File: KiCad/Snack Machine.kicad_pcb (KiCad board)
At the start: 2 copper layers, 107.5 x 100 mm, 314 parts, among them J1 MDB, J10 Row Screw Terminal, J11 Column Screw Terminal, J12 Display Serial Header, J13 RFID_CONNECTOR, J14 Large Display Header, J16 USB_B_Micro, J17 AVR-ISP-6, J18 Conn_02x02_Odd_Even, J2 Power Screw Terminal, J3 RFID Serial Connector, J4 RFID Led Connector, J5 MDB, J6 Conn_01x02, J7 LCD EXP1, J8 LCD EXP2, J9 AVR-ISP-6, Q1 P-CH 30V 3.8A, Q10 MMBT3904, Q11 P-CH 30V 3.8A, Q12 P-CH 30V 3.8A, Q13 P-CH 30V 3.8A, Q14 P-CH 30V 3.8A, Q15 MMBT3904, Q16 MMBT3904, Q17 MMBT3904, Q18 MMBT3904, Q19 Q_NMOS_SGD, Q2 Q_NMOS_SGD, Q20 Q_NMOS_SGD, Q21 Q_NMOS_SGD, Q22 Q_NMOS_SGD, Q23 Q_NMOS_SGD, Q24 Q_NMOS_SGD, Q25 Q_NMOS_SGD, Q3 P-CH 30V 3.8A, Q4 P-CH 30V 3.8A, Q5 P-CH 30V 3.8A, Q6 P-CH 30V 3.8A, Q7 MMBT3904, Q8 MMBT3904, Q9 MMBT3904, SW1 SW_SPST, U1 MEZD71201A-F, U2 MEZD71202A-G, U3 ATmega2560-16AU, U4 INA180B3, U5 INA219, U6 ATmega16U2-MU, U7 74AHC1G125, U8 W5500, U9 RB1-125BAG1A, Y1 16MHz, Y2 16MHz, Y3 25MHz

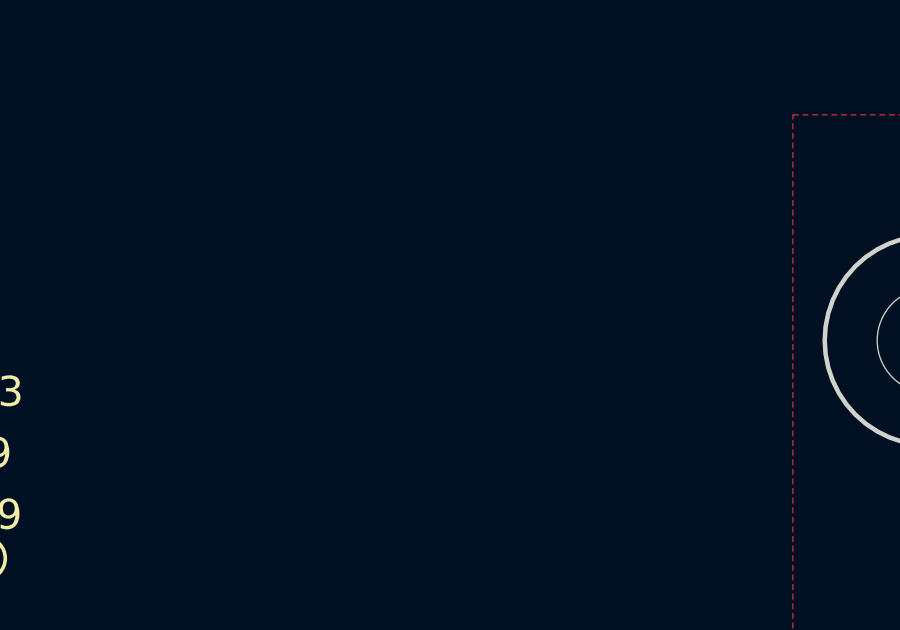
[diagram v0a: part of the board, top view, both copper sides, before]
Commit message: added one resistor, about to rip up all traces and move all the parts around
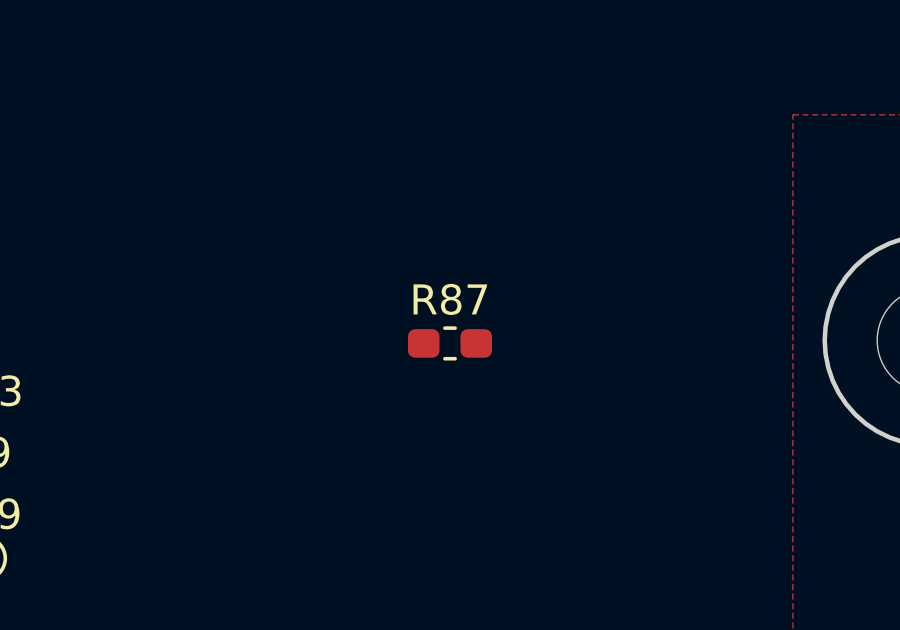
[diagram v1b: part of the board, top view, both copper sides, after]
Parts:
- added R87: OPEN, Resistor_SMD:R_0603_1608Metric_Pad1.05x0.95mm_HandSolder, F.Cu at (80.0, 57.1)
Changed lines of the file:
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@@
     (tracks 971)
     (zones 0)
-    (modules 314)
+    (modules 315)
     (nets 283)
   )
@@
       (at (xyz 0 0 0))
       (scale (xyz 1 1 1))
+      (rotate (xyz 0 0 0))
+    )
+  )
+  (module Resistor_SMD:R_0603_1608Metric_Pad1.05x0.95mm_HandSolder (layer F.Cu)
+    (at 80.01 57.15)
+    (descr "Resistor SMD 0603 (1608 Metric), square (rectangular) end terminal, IPC_7351 nominal with elongated pad for handsoldering. (Body size source: http://www.tortai-tech.com/upload/download/2011102023233369053.pdf), generated with kicad-footprint-generator")
+    (tags "resistor handsolder")
+    (attr smd)
+    (fp_text reference R87 (at 0 -1.43) (layer F.SilkS)
+      (effects (font (size 1 1) (thickness 0.15)))
+    )
+    (fp_text value OPEN (at 0 1.43) (layer F.Fab)
+      (effects (font (size 1 1) (thickness 0.15)))
+    )
+    (fp_line (start -0.8 0.4) (end -0.8 -0.4) (layer F.Fab) (width 0.1))
+    (fp_line (start -0.8 -0.4) (end 0.8 -0.4) (layer F.Fab) (width 0.1))
+    (fp_line (start 0.8 -0.4) (end 0.8 0.4) (layer F.Fab) (width 0.1))
+    (fp_line (start 0.8 0.4) (end -0.8 0.4) (layer F.Fab) (width 0.1))
+    (fp_line (start -0.171267 -0.51) (end 0.171267 -0.51) (layer F.SilkS) (width 0.12))
+    (fp_line (start -0.171267 0.51) (end 0.171267 0.51) (layer F.SilkS) (width 0.12))
+    (fp_line (start -1.65 0.73) (end -1.65 -0.73) (layer F.CrtYd) (width 0.05))
+    (fp_line (start -1.65 -0.73) (end 1.65 -0.73) (layer F.CrtYd) (width 0.05))
+    (fp_line (start 1.65 -0.73) (end 1.65 0.73) (layer F.CrtYd) (width 0.05))
+    (fp_line (start 1.65 0.73) (end -1.65 0.73) (layer F.CrtYd) (width 0.05))
+    (fp_text user %R (at 0 0) (layer F.Fab)
+      (effects (font (size 0.4 0.4) (thickness 0.06)))
+    )
+    (pad 1 smd roundrect (at -0.875 0) (size 1.05 0.95) (layers F.Cu F.Paste F.Mask) (roundrect_rratio 0.25)
+      (net 53 /MISO))
+    (pad 2 smd roundrect (at 0.875 0) (size 1.05 0.95) (layers F.Cu F.Paste F.Mask) (roundrect_rratio 0.25)
+      (net 214 /Ethernet/MISO_TRISTATE))
+    (model ${KISYS3DMOD}/Resistor_SMD.3dshapes/R_0603_1608Metric.wrl
+      (at (xyz 0 0 0))
+      (scale (xyz 1 1 1))

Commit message: rearranging footprints on layout
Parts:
- TP1, TP10, TP11, TP12, TP13, TP14, TP15, TP16, TP17, TP18, TP19, TP2, TP20, TP21, TP22, TP23, TP24, TP25, TP26, TP27, TP28, TP29, TP3, TP30, TP31, TP32, TP33, TP34, TP35, TP36, TP37, TP38, TP39, TP4, TP40, TP41, TP42, TP43, TP44, TP45, TP46, TP47, TP48, TP49, TP5, TP50, TP51, TP52, TP53, TP54, TP55, TP56, TP57, TP58, TP59, TP6, TP60, TP61, TP62, TP63, TP64, TP65, TP66, TP67, TP68, TP69, TP7, TP70, TP71, TP72, TP73, TP74, TP75, TP76, TP77, TP78, TP79, TP8, TP80, TP81, TP82, TP83, TP84, TP85, TP86, TP87, TP88, TP89, TP9, TP90, TP91, TP92, TP93: footprint TestPoint:TestPoint_THTPad_D1.0mm_Drill0.5mm -> Snack Machine:TestPoint_THTPad_D0.8mm_Drill0.4mm
- moved C45 194.5 mm to (66.3, 74.2)
- moved Y3 191.1 mm to (57.7, 123.2)
- moved R80 185.2 mm to (81.0, 173.5)
- moved R81 185.2 mm to (84.3, 172.0)
- moved R82 185.2 mm to (81.0, 175.0)
- moved R83 185.2 mm to (84.3, 173.5)
- moved R85 185.2 mm to (84.3, 175.0)
- moved R84 185.2 mm to (87.7, 172.0)
- moved R86 185.2 mm to (87.7, 173.5)
- moved R79 184.6 mm to (80.6, 170.8)
- moved FB2 183.4 mm to (70.2, 126.5)
- moved FB3 175.7 mm to (77.9, 126.2)
- moved TP1 162.8 mm to (108.1, 40.9)
- moved D4 159.2 mm to (280.7, 148.2)
- moved R59 159.2 mm to (285.9, 152.1)
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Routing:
- net +5V: track 106.7 -> 0.00 mm, vias 1 -> 0
- net /SCL: track 87.9 -> 0.00 mm, vias 3 -> 0
- net /SDA: track 82.3 -> 0.00 mm, vias 3 -> 0
- net /r1: track 70.3 -> 0.00 mm
- net /MOSI: track 65.9 -> 0.00 mm, vias 2 -> 0
- net /r2: track 65.1 -> 0.00 mm
- net /SCK: track 63.3 -> 0.00 mm, vias 2 -> 0
- net GND: track 62.8 -> 0.00 mm, vias 3 -> 0
- net /r3: track 62.2 -> 0.00 mm
- net /DOOR_SW: track 60.7 -> 0.00 mm, vias 1 -> 0
- net /r4: track 56.1 -> 0.00 mm
- net /r5: track 51.5 -> 0.00 mm
- net +24V: track 51.0 -> 0.00 mm
- net Net-(C7-Pad1): track 47.1 -> 0.00 mm, vias 1 -> 0
- net Net-(C9-Pad1): track 46.4 -> 0.00 mm, vias 1 -> 0
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
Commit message: moving stuff around
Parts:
- C45, R65, R74, R76, R87, U7: moved to B.Cu
- U1, U2: footprint Connector_PinHeader_2.54mm:PinHeader_1x03_P2.54mm_Vertical -> Snack Machine:mEZD71201A
- moved C24 229.7 mm to (32.7, 145.4)
- moved C27 229.7 mm to (34.2, 140.3)
- moved C29 229.7 mm to (40.2, 146.9)
- moved D4 229.7 mm to (51.0, 149.9)
- moved J17 229.7 mm to (56.0, 140.6)
- moved R59 229.7 mm to (56.2, 153.8)
- moved R60 229.7 mm to (56.2, 152.0)
- moved U6 229.7 mm to (38.8, 141.8)
- moved C18 229.7 mm to (61.1, 153.9)
- moved C20 229.7 mm to (61.1, 152.0)
- moved C23 229.7 mm to (33.2, 152.2)
- moved C25 229.7 mm to (40.8, 152.2)
- moved C26 229.7 mm to (30.6, 145.4)
- moved C28 229.7 mm to (40.8, 148.8)
- moved C30 229.7 mm to (51.5, 144.4)
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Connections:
- Y3 pad 2: Net-(C32-Pad1) -> GND
- Y3 pad 3: (no net) -> Net-(C32-Pad1)
- Y3 pad 4: (no net) -> GND

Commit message: Moved stuff around on the layout, still need to fanout the large processor, place the power regulators, place the door switch connector, place the RFID connectors, and place the LCD connectors.  Once all parts are placed, routing can begin.
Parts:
- C23, C25, C27, C28, C29, C46, C47, C48, C49, C50, C51, C52, C53, D5, D6, R55, R56, R57, R59, R60, R61, R62, R63, R79, R80, R81, R82, R83, R84, R85, R86, U6, Y2: moved to B.Cu
- moved C1 154.5 mm to (85.6, 129.2)
- moved C3 154.5 mm to (72.9, 129.2)
- moved D7 154.5 mm to (78.2, 124.3)
- moved TP85 154.5 mm to (86.7, 134.6)
- moved TP87 154.5 mm to (89.0, 134.0)
- moved D8 154.5 mm to (78.4, 121.7)
- moved U2 154.5 mm to (81.8, 127.9)
- moved R82 132.8 mm to (180.1, 86.7), turned to 180 degrees
- moved R85 129.7 mm to (182.9, 90.8), turned to 270 degrees
- moved R86 129.4 mm to (182.9, 85.9), turned to 270 degrees
- moved R80 125.4 mm to (180.1, 96.6), turned to 180 degrees
- moved R81 125.0 mm to (180.1, 91.7), turned to 180 degrees
- moved R83 122.5 mm to (182.9, 100.8), turned to 270 degrees
- moved R84 122.0 mm to (182.9, 95.8), turned to 270 degrees
- moved R79 121.1 mm to (180.1, 101.7)
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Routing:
- net /r8: vias 1 -> 0
- net /r7: vias 1 -> 0
- net /r6: vias 1 -> 0
- net /r5: vias 1 -> 0
- net /r4: vias 1 -> 0
- net /r3: vias 1 -> 0
- net /r2: vias 1 -> 0
- net /r1: vias 1 -> 0
- net /c7: vias 1 -> 0
- net /c6: vias 1 -> 0
- net /c5: vias 1 -> 0
- net /c4: vias 1 -> 0
- net /c3: vias 1 -> 0
- net /c2: vias 1 -> 0
- net /c1: vias 1 -> 0
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
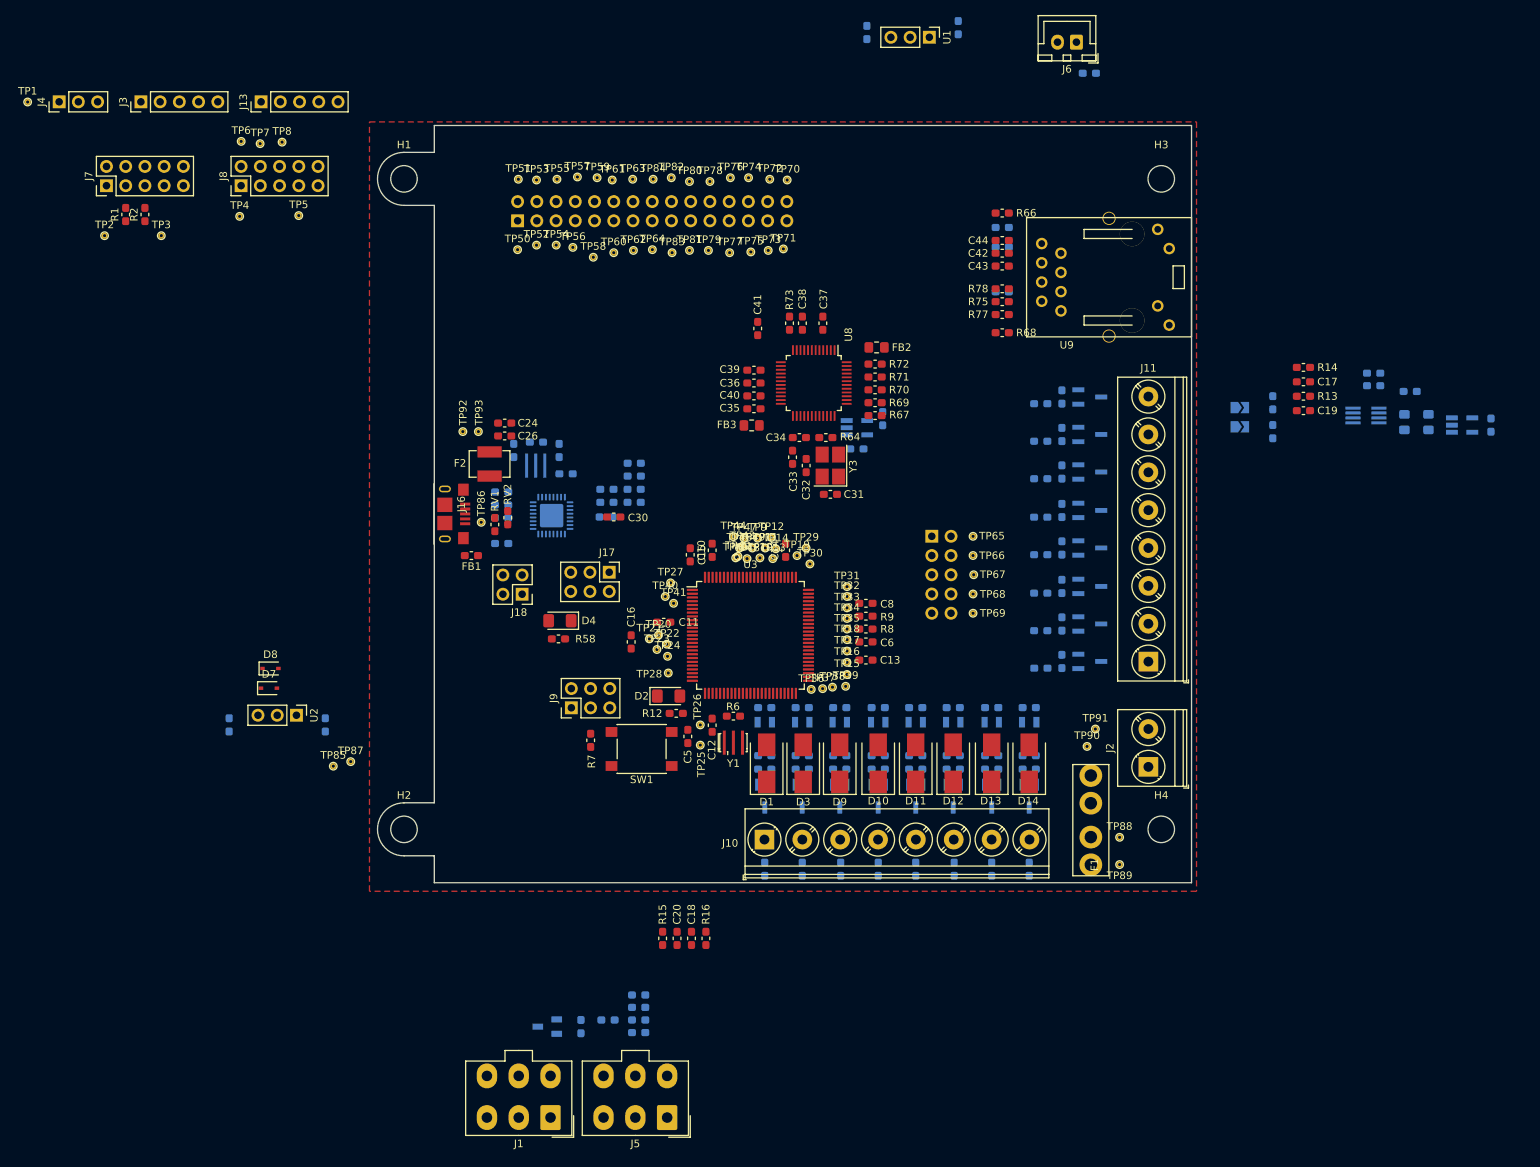
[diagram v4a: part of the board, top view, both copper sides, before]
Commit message: all parts placed within board outline
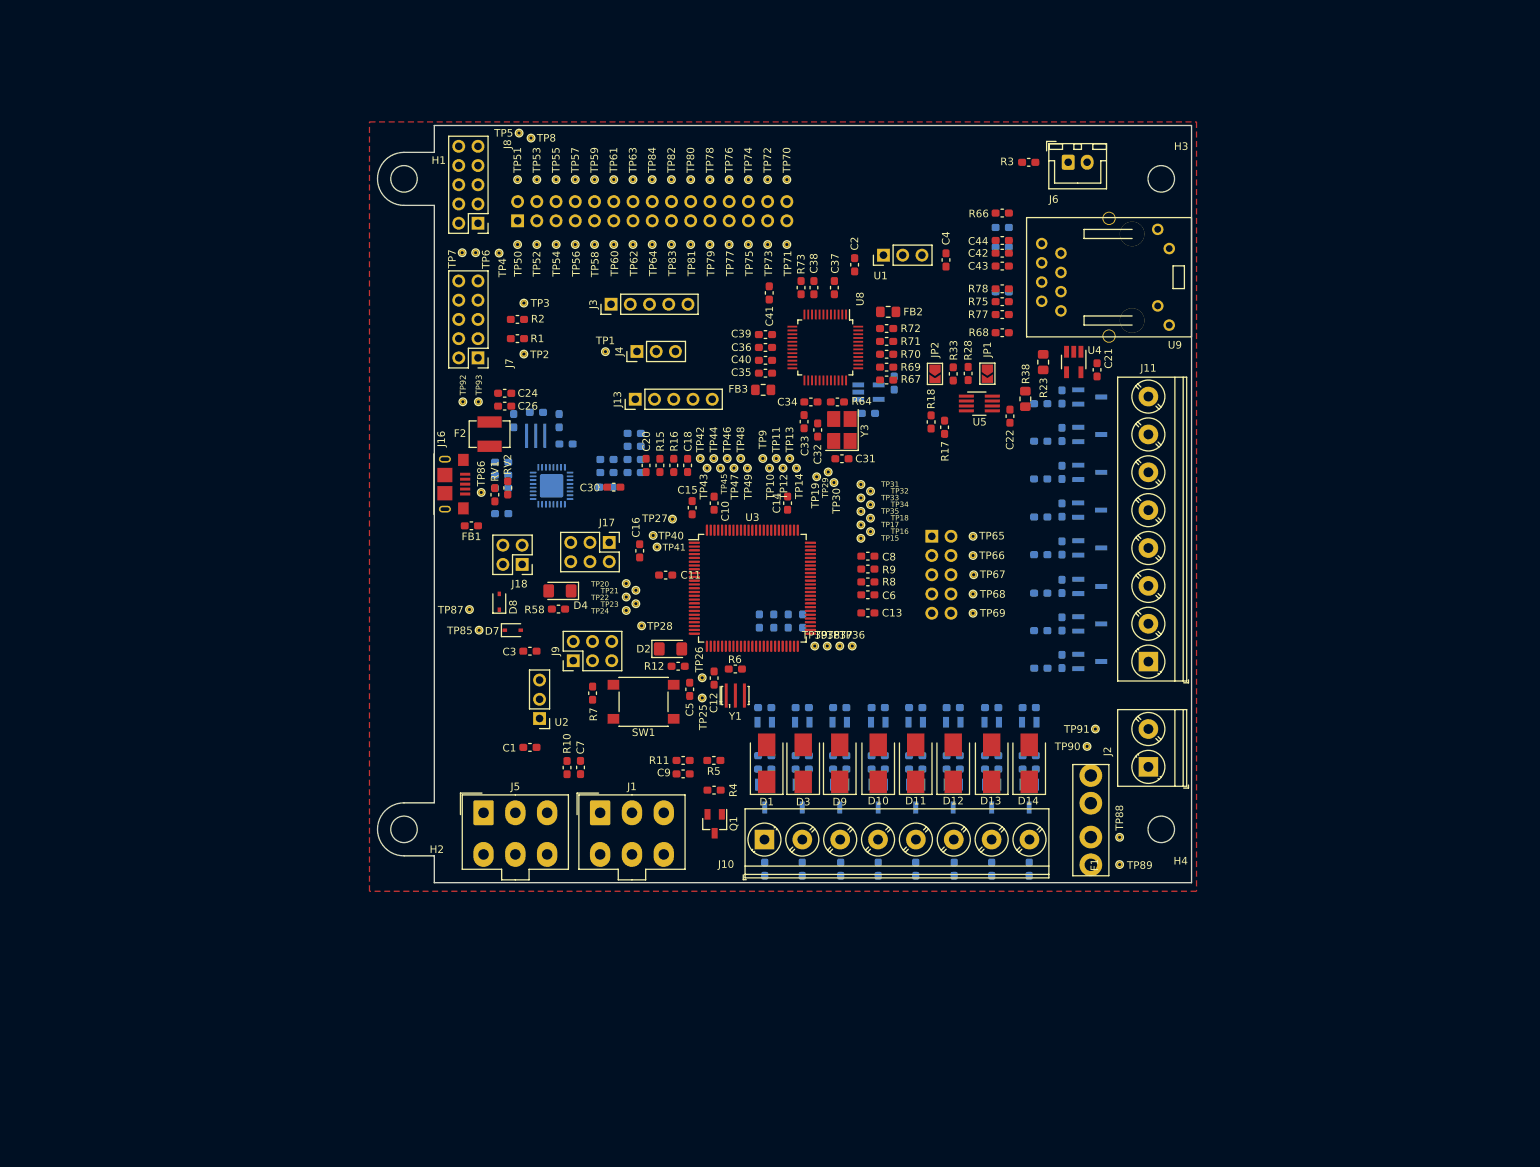
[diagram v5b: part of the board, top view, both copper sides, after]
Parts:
- C1, C2, C21, C22, C3, C4, C7, C9, JP1, JP2, Q1, R10, R11, R17, R18, R23, R28, R3, R33, R38, R4, R5, U4, U5: moved to F.Cu
- C17, C19, R13, R14: moved to B.Cu
- moved J4 83.1 mm to (126.8, 79.8)
- moved TP1 83.1 mm to (122.6, 79.9)
- moved C19 77.0 mm to (142.9, 115.4), turned to 90 degrees
- moved R13 76.0 mm to (144.8, 115.4), turned to 270 degrees
- moved C17 75.0 mm to (146.7, 115.4), turned to 90 degrees
- moved R14 74.1 mm to (148.6, 115.4), turned to 270 degrees
- moved J3 67.6 mm to (123.3, 73.6)
- moved J13 63.1 mm to (126.5, 86.2)
- moved R16 62.6 mm to (131.6, 94.9), turned to 270 degrees
- moved C20 62.6 mm to (128.0, 94.9), turned to 90 degrees
- moved C18 62.5 mm to (133.5, 94.9), turned to 90 degrees
- moved R15 62.5 mm to (129.8, 94.9), turned to 270 degrees
- moved R18 58.6 mm to (165.6, 89.2), turned to 90 degrees
- moved TP2 57.5 mm to (111.8, 80.2), turned to 90 degrees
- moved R17 57.1 mm to (167.4, 89.9), turned to 90 degrees
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
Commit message: some routing complete
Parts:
- moved C19 17.9 mm to (160.5, 112.3)
- moved R13 17.9 mm to (162.4, 112.3)
- moved C17 15.4 mm to (160.5, 108.5)
- moved R14 15.4 mm to (162.4, 108.5)
- moved TP1 15.1 mm to (137.7, 80.1), turned to 180 degrees
- moved R10 13.0 mm to (104.6, 135.1)
- moved C7 13.0 mm to (106.4, 135.1)
- moved TP25 9.74 mm to (129.0, 118.2)
- moved J4 6.81 mm to (133.6, 80.1), turned to 270 degrees
- moved TP26 5.85 mm to (130.7, 119.5)
- moved TP36 2.71 mm to (157.3, 120.5)
- moved TP37 2.70 mm to (155.4, 120.7)
- moved D2 2.49 mm to (131.2, 121.6)
- moved R12 2.49 mm to (132.2, 123.9)
- moved TP90 2.47 mm to (187.6, 129.9)
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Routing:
- net GND: track 0.00 -> 708.9 mm, vias 0 -> 12
- net +24V: track 0.00 -> 220.2 mm, vias 0 -> 8
- net +5V: track 0.00 -> 175.4 mm, vias 0 -> 5
- net VCC: track 0.00 -> 85.8 mm
- net /MotorPower/motor_common_gnd: track 0.00 -> 78.2 mm, vias 0 -> 9
- net /DOOR_SW: track 0.00 -> 75.5 mm, vias 0 -> 1
- net /c8: track 0.00 -> 58.5 mm, vias 0 -> 1
- net /c7: track 0.00 -> 54.8 mm, vias 0 -> 1
- net /c6: track 0.00 -> 51.0 mm, vias 0 -> 1
- net /c5: track 0.00 -> 47.0 mm, vias 0 -> 1
- net Net-(C7-Pad1): track 0.00 -> 45.1 mm, vias 0 -> 2
- net /c4: track 0.00 -> 43.1 mm, vias 0 -> 1
- net /r8: track 0.00 -> 40.2 mm, vias 0 -> 1
- net /c3: track 0.00 -> 39.4 mm, vias 0 -> 1
- net /r7: track 0.00 -> 35.8 mm, vias 0 -> 1
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- added copper zone on B.Cu, net (none)
- removed copper zone on F.Cu, net GND
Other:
- net class High Amp: trace_width 0.781437 -> 0.8
- net class Signal added: clearance 0.2, trace_width 0.25, via_dia 0.6, via_drill 0.3

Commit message: routed some more
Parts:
- moved TP92 25.5 mm to (106.7, 111.8)
- moved C18 5.55 mm to (127.9, 94.9)
- moved C20 5.53 mm to (133.5, 94.9)
- moved R55 4.23 mm to (113.4, 92.1)
- moved TP26 4.12 mm to (126.6, 119.9)
- moved TP4 3.02 mm to (105.5, 66.9)
- moved TP25 2.49 mm to (126.6, 118.5)
- moved Y2 1.93 mm to (113.4, 89.1)
- moved R15 1.84 mm to (131.6, 94.9)
- moved R16 1.82 mm to (129.8, 94.9)
- moved TP6 1.63 mm to (103.8, 66.9)
- moved TP7 1.63 mm to (102.1, 66.9)
- moved J18 1.51 mm to (112.8, 107.1)
- moved TP21 1.26 mm to (127.7, 112.1)
- moved TP23 1.26 mm to (127.7, 113.8)
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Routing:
- net GND: track 708.9 -> 821.2 mm, vias 12 -> 17
- net +5V: track 175.4 -> 232.3 mm, vias 5 -> 7
- net /USB_Serial/USBVCC: track 0.00 -> 46.8 mm
- net Net-(C9-Pad1): track 1.78 -> 47.9 mm, vias 0 -> 2
- net /RESET_DISPLAY: track 0.00 -> 27.7 mm, vias 0 -> 1
- net /USB_Serial/USB_SHIELD: track 0.00 -> 25.6 mm
- net /USB_Serial/SCK2: track 0.00 -> 24.9 mm
- net /USB_Serial/~RESET2: track 10.2 -> 33.6 mm
- net /USB_Serial/MOSI2: track 0.00 -> 18.1 mm
- net /USB_Serial/USB_GND: track 0.00 -> 15.1 mm, vias 0 -> 1
- net Net-(C18-Pad1): track 0.00 -> 14.9 mm
- net Net-(C20-Pad1): track 0.00 -> 14.5 mm
- net /USB_Serial/MICRO_TX: track 0.00 -> 10.6 mm
- net /USB_Serial/8PB6: track 0.00 -> 9.97 mm
- net /USB_Serial/MICRO_RX: track 0.00 -> 9.76 mm
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
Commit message: pushing stuff around, routing more
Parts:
- moved C39 0.95 mm to (143.1, 76.9), turned to 180 degrees
- moved C36 0.76 mm to (143.1, 78.9)
- moved C40 0.67 mm to (143.1, 80.8)
- moved C35 0.63 mm to (143.1, 82.7)
- moved JP1 0.50 mm to (172.5, 82.8)
- moved JP2 0.50 mm to (165.6, 82.8)
- moved R28 0.50 mm to (170.0, 82.8)
- moved R33 0.50 mm to (168.0, 82.8)
- moved C38 0.17 mm to (150.3, 71.4)
- moved R77 0.13 mm to (175.0, 75.1)
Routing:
- net GND: track 821.2 -> 941.1 mm, vias 17 -> 21
- net +5V: track 232.3 -> 324.4 mm, vias 7 -> 10
- net +3V3: track 3.27 -> 81.7 mm, vias 0 -> 2
- net /Ethernet/AGND: track 0.00 -> 66.0 mm, vias 0 -> 6
- net /Ethernet/AVDD: track 0.00 -> 47.3 mm, vias 0 -> 5
- net /Ethernet/TX+: track 0.00 -> 39.7 mm, vias 0 -> 1
- net /MOSI: track 15.4 -> 53.5 mm, vias 0 -> 1
- net /Ethernet/RX-: track 0.00 -> 37.1 mm, vias 0 -> 2
- net /SCK: track 27.3 -> 63.1 mm, vias 0 -> 1
- net /Ethernet/RX+: track 0.00 -> 34.2 mm, vias 0 -> 1
- net /Ethernet/TX-: track 0.00 -> 31.5 mm, vias 0 -> 1
- net /Ethernet/GREENLED: track 0.00 -> 26.0 mm, vias 0 -> 1
- net /Ethernet/YELLOWLED: track 0.00 -> 21.5 mm
- net /CS: track 0.00 -> 17.7 mm, vias 0 -> 1
- net Net-(C31-Pad1): track 0.00 -> 16.7 mm
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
